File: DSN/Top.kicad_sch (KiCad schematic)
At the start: 6 parts

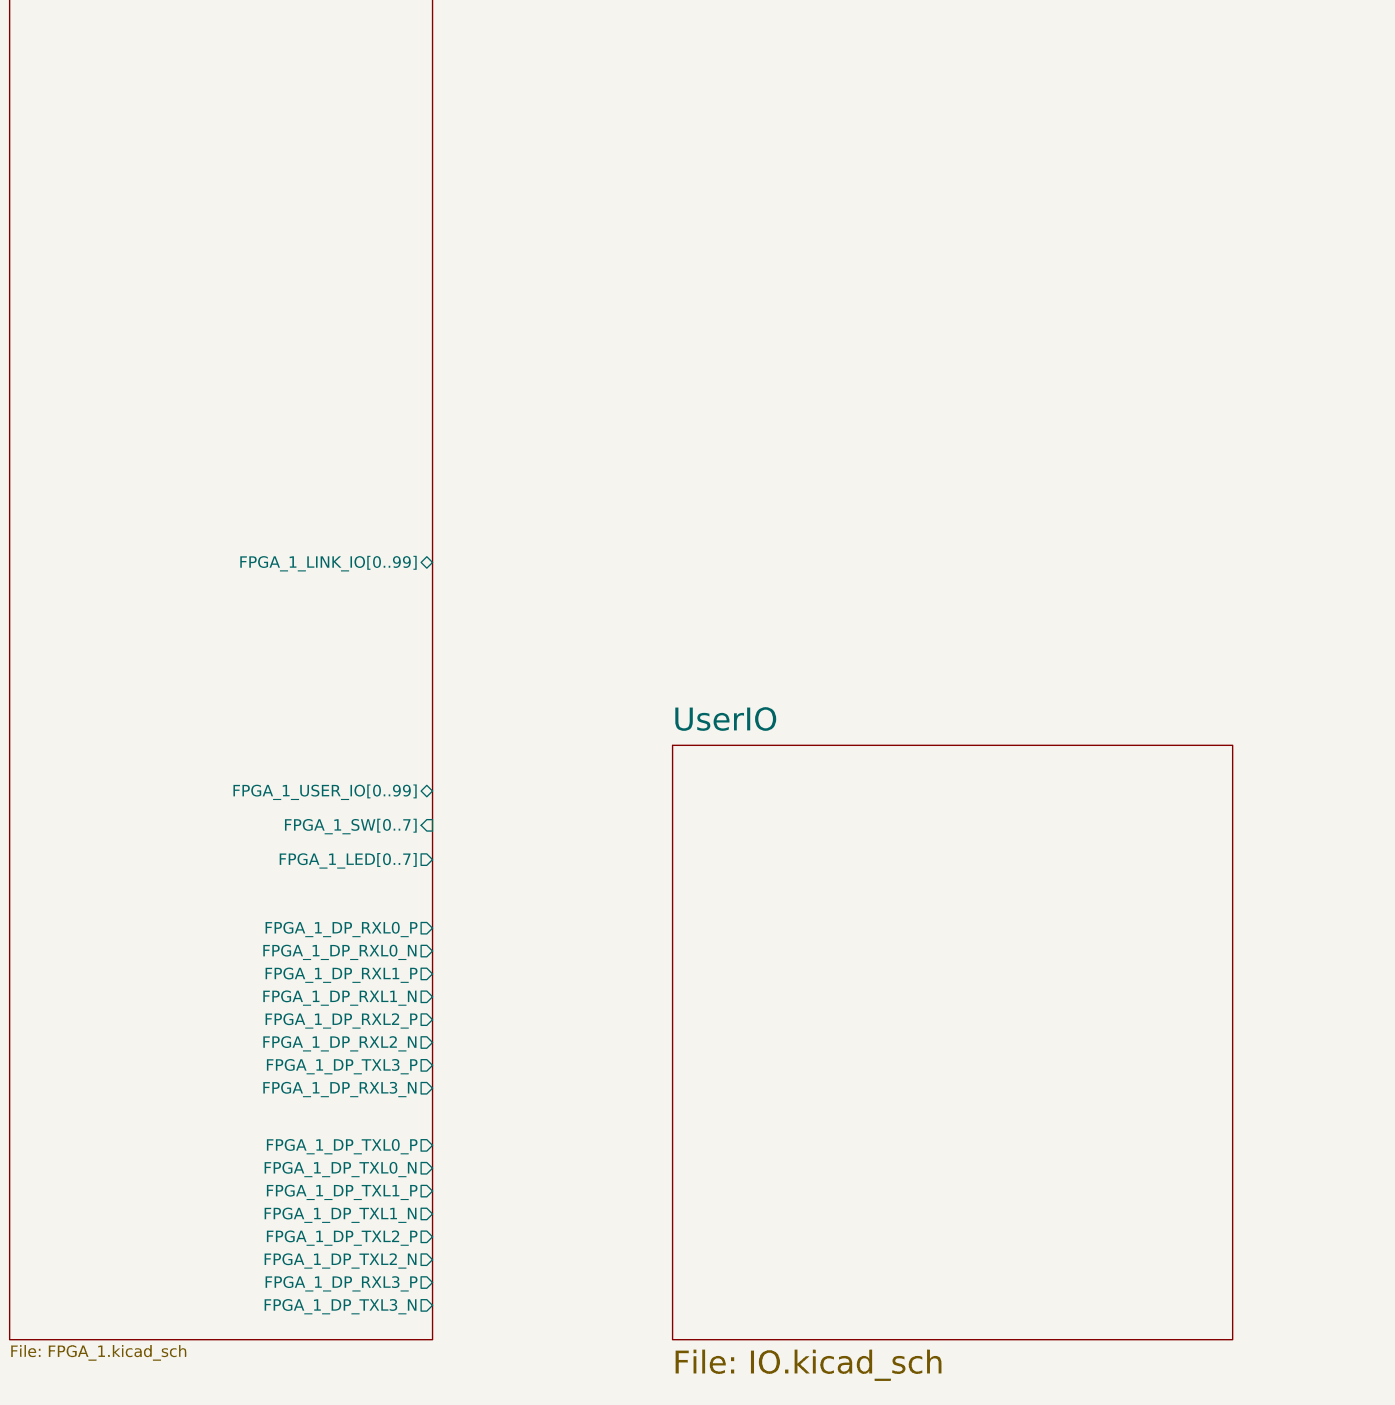
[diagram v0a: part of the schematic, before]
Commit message: Updates
Changed FPGA user io from 100 to 50 per chip, added 4 pmod per FPGA, added 8x buttons + led's, added SMA connectors for FPGA0 GTP.
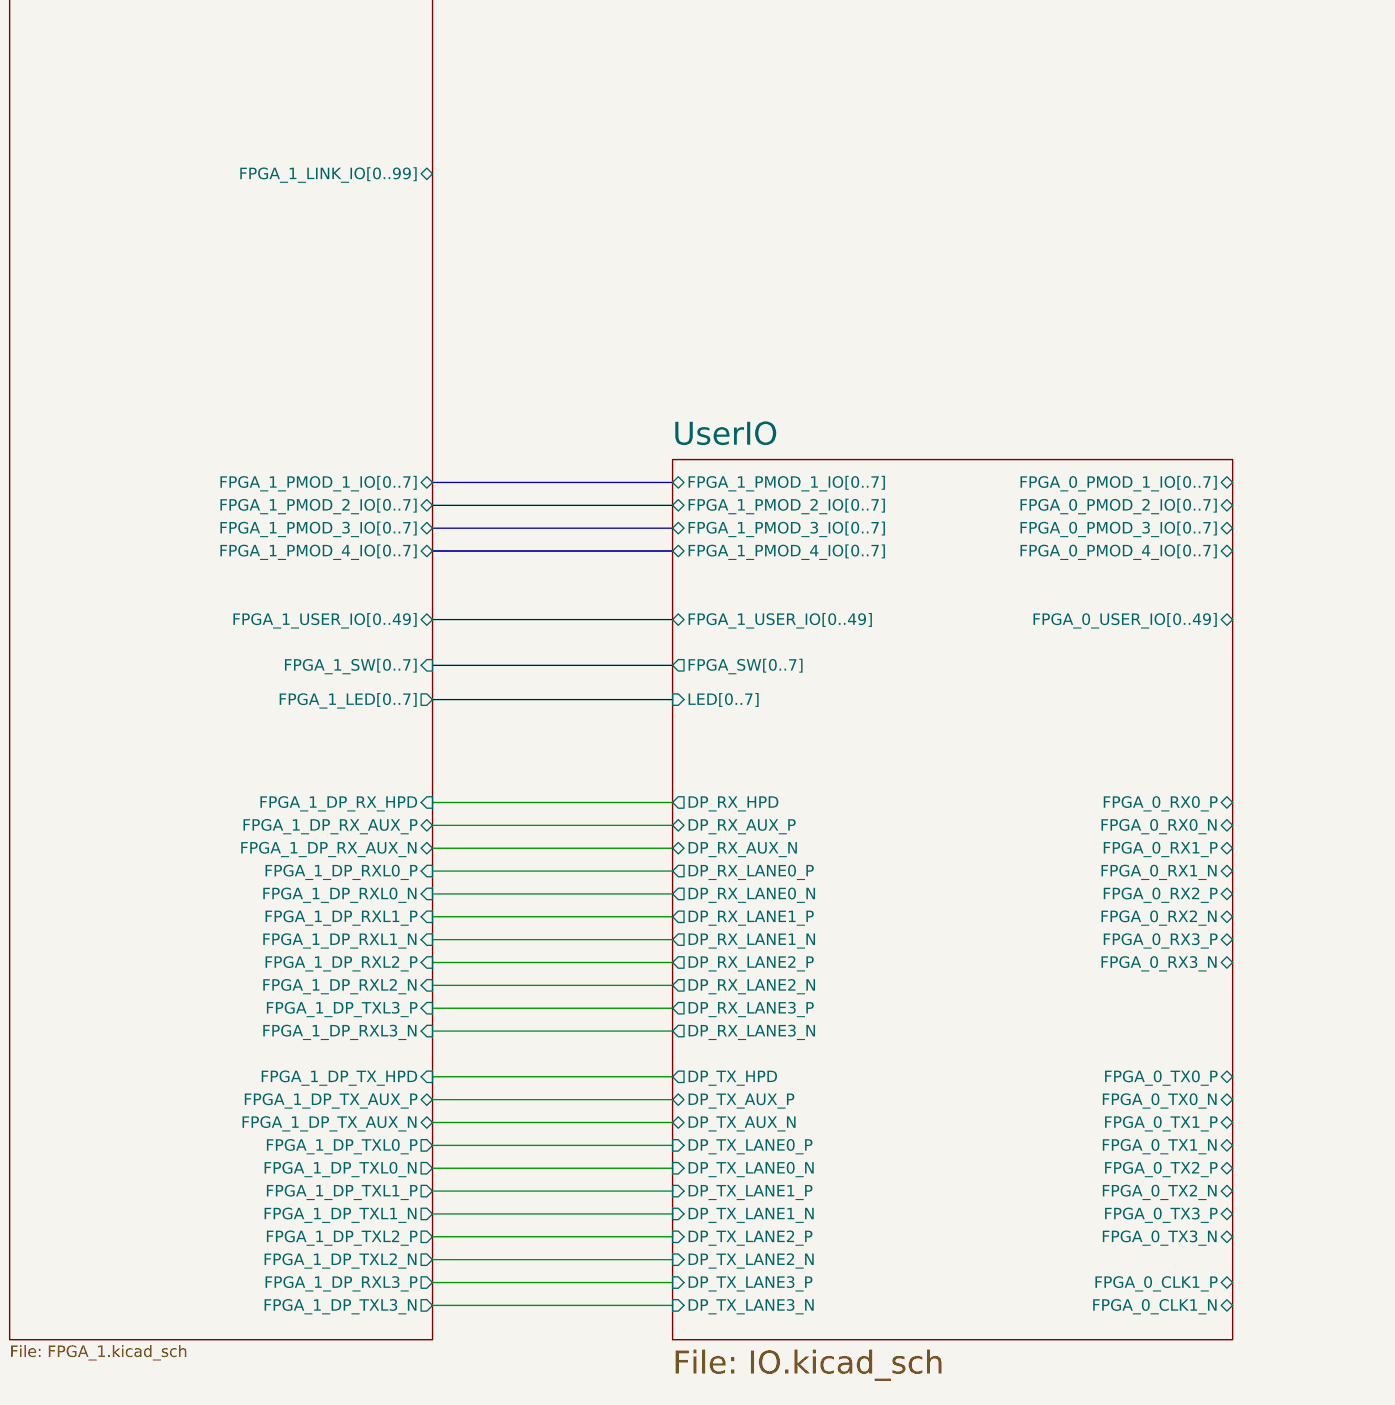
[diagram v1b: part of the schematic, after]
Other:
- sheet FPGA_1 ports: added FPGA_1_DP_RX_AUX_N, FPGA_1_DP_RX_AUX_P, FPGA_1_DP_RX_HPD, FPGA_1_DP_TX_AUX_N, FPGA_1_DP_TX_AUX_P, FPGA_1_DP_TX_HPD, FPGA_1_PMOD_1_IO[0..7], FPGA_1_PMOD_2_IO[0..7], FPGA_1_PMOD_3_IO[0..7], FPGA_1_PMOD_4_IO[0..7], FPGA_1_USER_IO[0..49]; removed FPGA_1_USER_IO[0..99]
- sheet UserIO ports: added DP_RX_AUX_N, DP_RX_AUX_P, DP_RX_HPD, DP_RX_LANE0_N, DP_RX_LANE0_P, DP_RX_LANE1_N, DP_RX_LANE1_P, DP_RX_LANE2_N, DP_RX_LANE2_P, DP_RX_LANE3_N, DP_RX_LANE3_P, DP_TX_AUX_N, DP_TX_AUX_P, DP_TX_HPD, DP_TX_LANE0_N, DP_TX_LANE0_P, DP_TX_LANE1_N, DP_TX_LANE1_P, DP_TX_LANE2_N, DP_TX_LANE2_P, DP_TX_LANE3_N, DP_TX_LANE3_P, FPGA_0_CLK1_N, FPGA_0_CLK1_P, FPGA_0_PMOD_1_IO[0..7], FPGA_0_PMOD_2_IO[0..7], FPGA_0_PMOD_3_IO[0..7], FPGA_0_PMOD_4_IO[0..7], FPGA_0_RX0_N, FPGA_0_RX0_P, FPGA_0_RX1_N, FPGA_0_RX1_P, FPGA_0_RX2_N, FPGA_0_RX2_P, FPGA_0_RX3_N, FPGA_0_RX3_P, FPGA_0_TX0_N, FPGA_0_TX0_P, FPGA_0_TX1_N, FPGA_0_TX1_P, FPGA_0_TX2_N, FPGA_0_TX2_P, FPGA_0_TX3_N, FPGA_0_TX3_P, FPGA_0_USER_IO[0..49], FPGA_1_PMOD_1_IO[0..7], FPGA_1_PMOD_2_IO[0..7], FPGA_1_PMOD_3_IO[0..7], FPGA_1_PMOD_4_IO[0..7], FPGA_1_USER_IO[0..49], FPGA_SW[0..7], LED[0..7]; removed none

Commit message: Added PSRAM, Finished Schematic
Footprint assignment required, some minor changes to be made to schematic. Sheet naming and commenting to be done.
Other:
- sheet DDR Memory renamed PSRAM Memory
- sheet FPGA_0 ports: added FPGA_0_GTP_CLK1_N, FPGA_0_GTP_CLK1_P, FPGA_0_LED[0..7], FPGA_0_LINK_IO[0..99], FPGA_0_MCU_IO[0..15], FPGA_0_PMOD0_IO[0..7], FPGA_0_PMOD1_IO[0..7], FPGA_0_PMOD2_IO[0..7], FPGA_0_PMOD3_IO[0..7], FPGA_0_PSRAM_CLK_N, FPGA_0_PSRAM_CLK_P, FPGA_0_PSRAM_CS, FPGA_0_PSRAM_D[0..7], FPGA_0_PSRAM_RESET, FPGA_0_PSRAM_RWDS, FPGA_0_RXL0_N, FPGA_0_RXL0_P, FPGA_0_RXL1_N, FPGA_0_RXL1_P, FPGA_0_RXL2_N, FPGA_0_RXL2_P, FPGA_0_RXL3_N, FPGA_0_RXL3_P, FPGA_0_SPI_MCU_CS, FPGA_0_SPI_MCU_RX, FPGA_0_SPI_MCU_SCLK, FPGA_0_SPI_MCU_TX, FPGA_0_SPI_SMC_CS, FPGA_0_SPI_SMC_RX, FPGA_0_SPI_SMC_SCLK, FPGA_0_SPI_SMC_TX, FPGA_0_SW[0..7], FPGA_0_TCK, FPGA_0_TDI, FPGA_0_TDO, FPGA_0_TMS, FPGA_0_TXL0_N, FPGA_0_TXL0_P, FPGA_0_TXL1_N, FPGA_0_TXL1_P, FPGA_0_TXL2_N, FPGA_0_TXL2_P, FPGA_0_TXL3_N, FPGA_0_TXL3_P, FPGA_0_UART_RX, FPGA_0_UART_TX, FPGA_0_USER_IO[0..49]; removed none
- sheet FPGA_1 ports: added FPGA_1_PMOD0_IO[0..7], FPGA_1_PMOD1_IO[0..7], FPGA_1_PMOD2_IO[0..7], FPGA_1_PMOD3_IO[0..7]; removed FPGA_1_PMOD_1_IO[0..7], FPGA_1_PMOD_2_IO[0..7], FPGA_1_PMOD_3_IO[0..7], FPGA_1_PMOD_4_IO[0..7]
- sheet PSRAM Memory: file DDR_Memory.kicad_sch -> PSRAM.kicad_sch
- sheet PSRAM Memory ports: added PSRAM_CLK_N, PSRAM_CLK_P, PSRAM_CS, PSRAM_DQ[0..7], PSRAM_RST, PSRAM_RWDS; removed none
- sheet UserIO ports: added FPGA_0_LED[0..7], FPGA_0_PMOD0_IO[0..7], FPGA_0_PMOD1_IO[0..7], FPGA_0_PMOD2_IO[0..7], FPGA_0_PMOD3_IO[0..7], FPGA_0_SW[0..7], FPGA_1_LED[0..7], FPGA_1_PMOD0_IO[0..7], FPGA_1_PMOD1_IO[0..7], FPGA_1_PMOD2_IO[0..7], FPGA_1_PMOD3_IO[0..7], FPGA_1_SW[0..7]; removed FPGA_0_PMOD_1_IO[0..7], FPGA_0_PMOD_2_IO[0..7], FPGA_0_PMOD_3_IO[0..7], FPGA_0_PMOD_4_IO[0..7], FPGA_1_PMOD_1_IO[0..7], FPGA_1_PMOD_2_IO[0..7], FPGA_1_PMOD_3_IO[0..7], FPGA_1_PMOD_4_IO[0..7], FPGA_SW[0..7], LED[0..7]
- moved on the sheet: C?

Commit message: Added component ref des
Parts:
- added H1, H2, H3, H4, H5, H6, H7, H8: MountingHole, MountingHole:MountingHole_3.5mm, symbol Mechanical:MountingHole
- gave numbers to parts that had none: 6
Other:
- sheet FPGA_0 ports: added TSNS_FPGA0; removed none
- sheet FPGA_1 ports: added TSNS_FPGA1; removed none
- sheet SMC ports: added none; removed SMC_TSNS_3
- sheet Teensy41 MCU ports: added MCU_SPI1_SCLK; removed MUC_SPI1_SCLK
- sheet USB_UART_JTAG ports: added FPGA_1_TCK, FPGA_1_TDI, FPGA_1_TDO; removed none

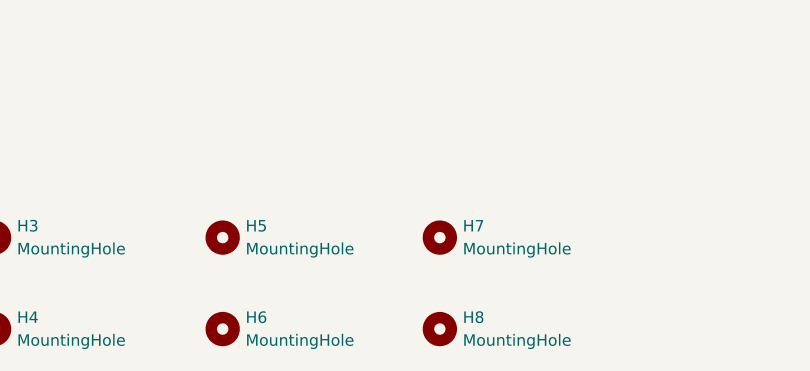
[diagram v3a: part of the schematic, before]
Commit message: Initial PCB Layout
Initial layout and part placement
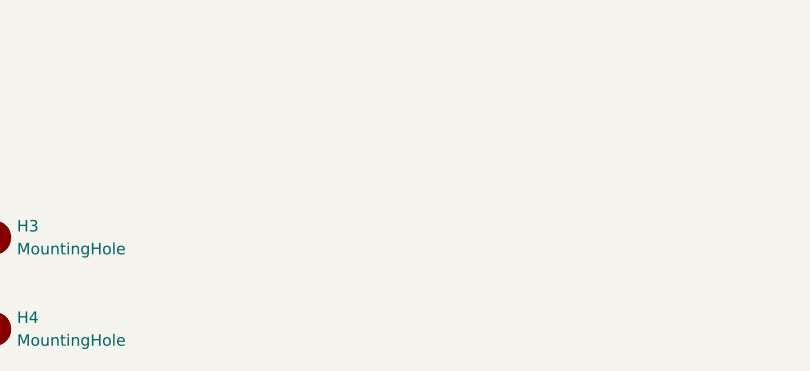
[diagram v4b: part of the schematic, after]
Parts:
- removed H5, H6, H7, H8: MountingHole, MountingHole:MountingHole_3.5mm, symbol Mechanical:MountingHole
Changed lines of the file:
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@@
     (pin "1")
-  )
-  (symbol (lib_id "Mechanical:MountingHole") (at 80.01 386.08 0) (unit 1)
-    (in_bom yes) (on_board yes) (fields_autoplaced)
-    (property "Reference" "H6" (id 0) (at 82.55 384.8099 0)
-      (effects (font (size 1.27 1.27)) (justify left))
-    )
-    (property "Value" "MountingHole" (id 1) (at 82.55 387.3499 0)
-      (effects (font (size 1.27 1.27)) (justify left))
-    )
-    (property "Footprint" "MountingHole:MountingHole_3.5mm" (id 2) (at 80.01 386.08 0)
-      (effects (font (size 1.27 1.27)) hide)
-    )
-    (property "Datasheet" "~" (id 3) (at 80.01 386.08 0)
-      (effects (font (size 1.27 1.27)) hide)
-    )
   )
   (symbol (lib_id "power:GND") (at 69.85 101.6 0) (unit 1)
@@
     (pin "1")
   )
-  (symbol (lib_id "Mechanical:MountingHole") (at 104.14 386.08 0) (unit 1)
-    (in_bom yes) (on_board yes) (fields_autoplaced)
-    (property "Reference" "H8" (id 0) (at 106.68 384.8099 0)
-      (effects (font (size 1.27 1.27)) (justify left))
-    )
-    (property "Value" "MountingHole" (id 1) (at 106.68 387.3499 0)
-      (effects (font (size 1.27 1.27)) (justify left))
-    )
-    (property "Footprint" "MountingHole:MountingHole_3.5mm" (id 2) (at 104.14 386.08 0)
-      (effects (font (size 1.27 1.27)) hide)
-    )
-    (property "Datasheet" "~" (id 3) (at 104.14 386.08 0)
-      (effects (font (size 1.27 1.27)) hide)
-    )
-  )
-  (symbol (lib_id "Mechanical:MountingHole") (at 80.01 375.92 0) (unit 1)
-    (in_bom yes) (on_board yes) (fields_autoplaced)
-    (property "Reference" "H5" (id 0) (at 82.55 374.6499 0)
-      (effects (font (size 1.27 1.27)) (justify left))
-    )
-    (property "Value" "MountingHole" (id 1) (at 82.55 377.1899 0)
-      (effects (font (size 1.27 1.27)) (justify left))
-    )
-    (property "Footprint" "MountingHole:MountingHole_3.5mm" (id 2) (at 80.01 375.92 0)
-      (effects (font (size 1.27 1.27)) hide)
-    )
-    (property "Datasheet" "~" (id 3) (at 80.01 375.92 0)
-      (effects (font (size 1.27 1.27)) hide)
-    )
-  )
-  (symbol (lib_id "Mechanical:MountingHole") (at 104.14 375.92 0) (unit 1)
-    (in_bom yes) (on_board yes) (fields_autoplaced)
-    (property "Reference" "H7" (id 0) (at 106.68 374.6499 0)
-      (effects (font (size 1.27 1.27)) (justify left))
-    )
-    (property "Value" "MountingHole" (id 1) (at 106.68 377.1899 0)
-      (effects (font (size 1.27 1.27)) (justify left))
-    )
-    (property "Footprint" "MountingHole:MountingHole_3.5mm" (id 2) (at 104.14 375.92 0)
-      (effects (font (size 1.27 1.27)) hide)
-    )
-    (property "Datasheet" "~" (id 3) (at 104.14 375.92 0)
-      (effects (font (size 1.27 1.27)) hide)
-    )
-  )
   (symbol (lib_id "Device:C_Small") (at 46.99 95.25 0) (unit 1)

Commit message: Updated Layout
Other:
- sheet Teensy41 MCU renamed RP2040 MCU
- sheet FPGA_0 ports: added FPGA_0_MCU_IO[0..8], FPGA_0_SW[0..3], SMC_IO0, SMC_IO1; removed FPGA_0_MCU_IO[0..15], FPGA_0_SPI_MCU_CS, FPGA_0_SPI_MCU_RX, FPGA_0_SPI_MCU_SCLK, FPGA_0_SPI_MCU_TX, FPGA_0_SW[0..7]
- sheet FPGA_1 ports: added FPGA_1_MCU_IO[0..8], FPGA_1_SW[0..3], SMC_IO2, SMC_IO3; removed FPGA_1_MCU_IO[0..15], FPGA_1_SPI_MCU_CS, FPGA_1_SPI_MCU_RX, FPGA_1_SPI_MCU_SCLK, FPGA_1_SPI_MCU_TX, FPGA_1_SW[0..7]
- sheet RP2040 MCU: file T41_MCU.kicad_sch -> RP2040_MCU.kicad_sch
- sheet RP2040 MCU ports: added FPGA_0_GPIO[0..8], FPGA_1_GPIO[0..8], SMC_3V3_AUX; removed MCU_FPGA_0_IO[0..15], MCU_FPGA_1_IO[0..15], MCU_SPI0_CS, MCU_SPI0_RX, MCU_SPI0_SCLK, MCU_SPI0_TX, MCU_SPI1_CS, MCU_SPI1_RX, MCU_SPI1_SCLK, MCU_SPI1_TX
- sheet SMC ports: added SMC_IO0, SMC_IO1, SMC_IO2, SMC_IO3; removed none
- sheet UserIO ports: added FPGA_0_SW[0..3], FPGA_1_SW[0..3]; removed FPGA_0_SW[0..7], FPGA_1_SW[0..7]

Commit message: Layout Update
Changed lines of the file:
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@@
+    (stroke (width 0) (type default) (color 0 0 0 0))
+  )
+  (wire (pts (xy 266.7 345.44) (xy 293.37 345.44))
     (stroke (width 0) (type default) (color 0 0 0 0))
   )
@@
   )
   (wire (pts (xy 194.31 90.17) (xy 402.59 90.17))
-    (stroke (width 0) (type default) (color 0 0 0 0))
-  )
-  (wire (pts (xy 266.7 345.44) (xy 293.37 345.44))
     (stroke (width 0) (type default) (color 0 0 0 0))
   )
@@
       (effects (font (size 1.27 1.27)) (justify right))
     )
-    (pin "FPGA_1_DP_TXL3_P" input (at 266.7 314.96 0)
+    (pin "FPGA_1_DP_TXL3_P" output (at 266.7 345.44 0)
       (effects (font (size 1.27 1.27)) (justify right))
     )
@@
       (effects (font (size 1.27 1.27)) (justify right))
     )
-    (pin "FPGA_1_DP_RXL3_P" output (at 266.7 345.44 0)
-      (effects (font (size 1.27 1.27)) (justify right))
-    )
+    (pin "FPGA_1_DP_RXL3_P" input (at 266.7 314.96 0)
+      (effects (font (size 1.27 1.27)) (justify right))
+    )
